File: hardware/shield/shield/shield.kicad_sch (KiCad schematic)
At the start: 4 parts, among them J3 Analog, J4 Digital/PWM, P1 Digital/PWM

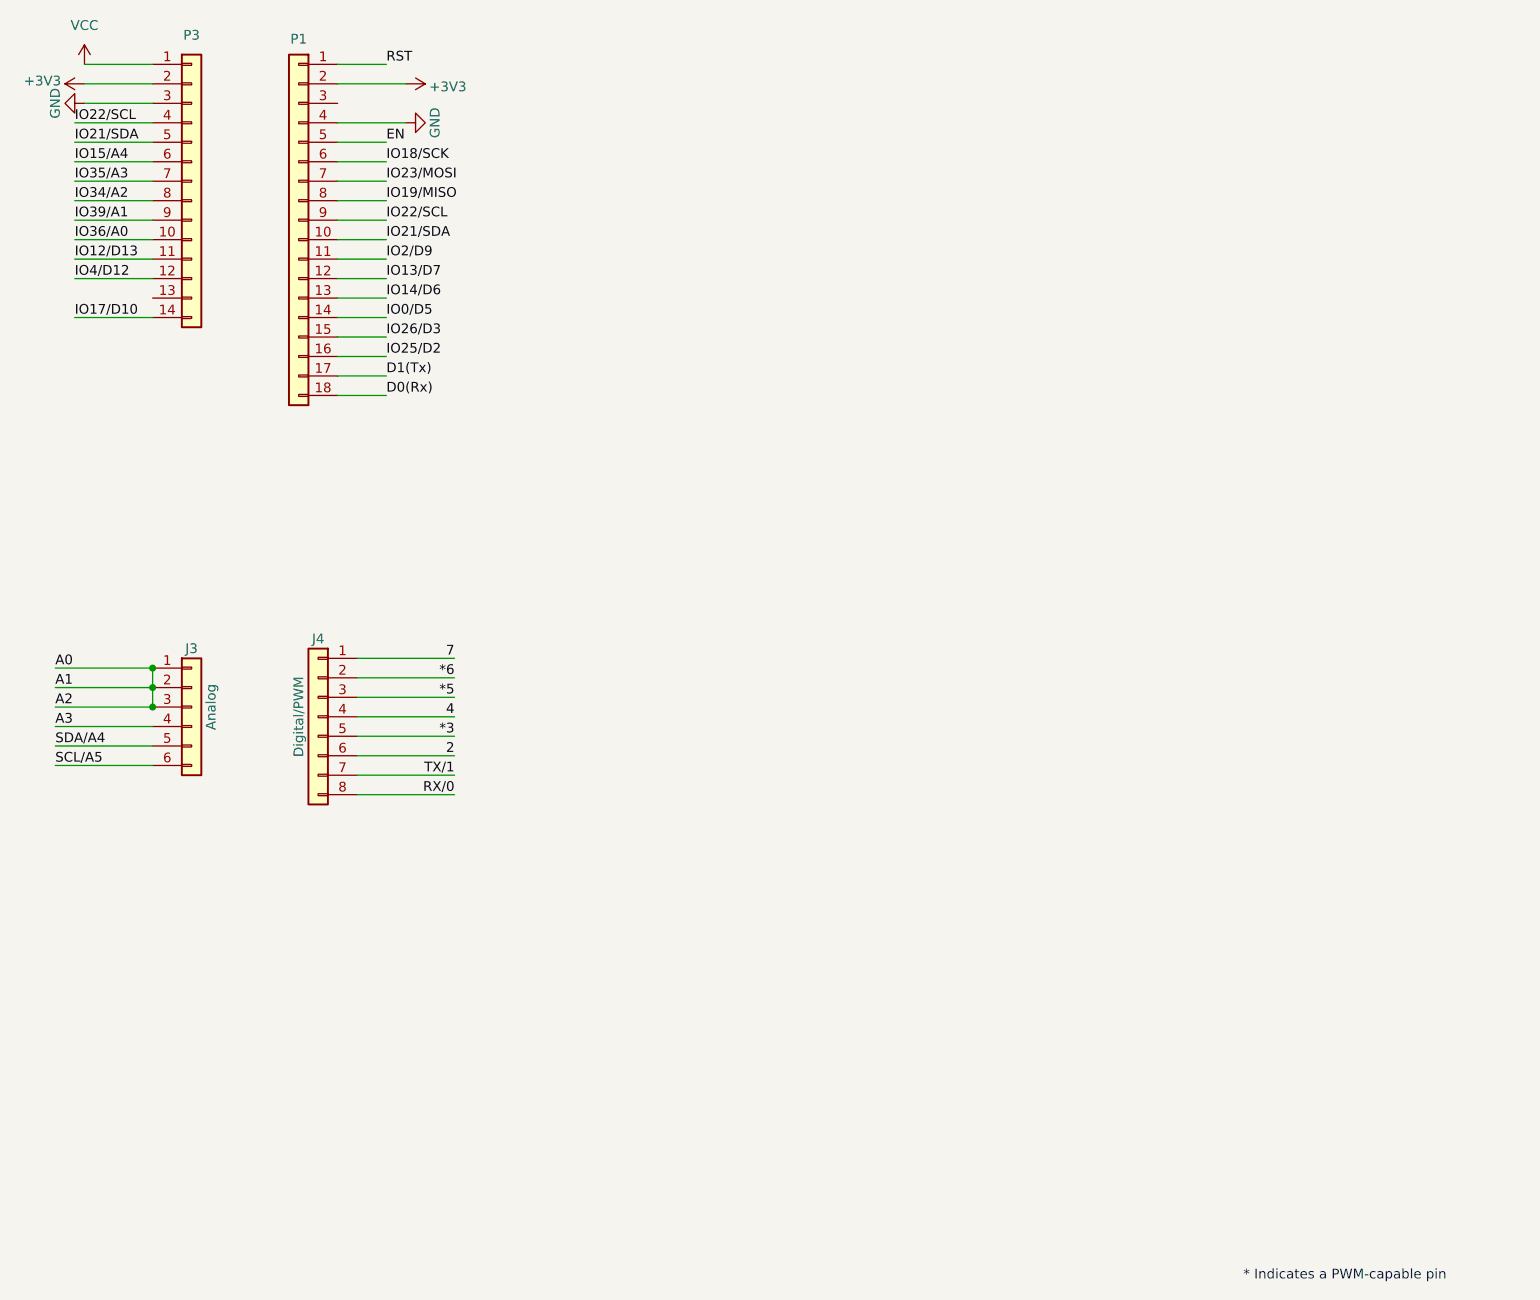
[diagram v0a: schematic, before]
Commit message: add pins for in/out
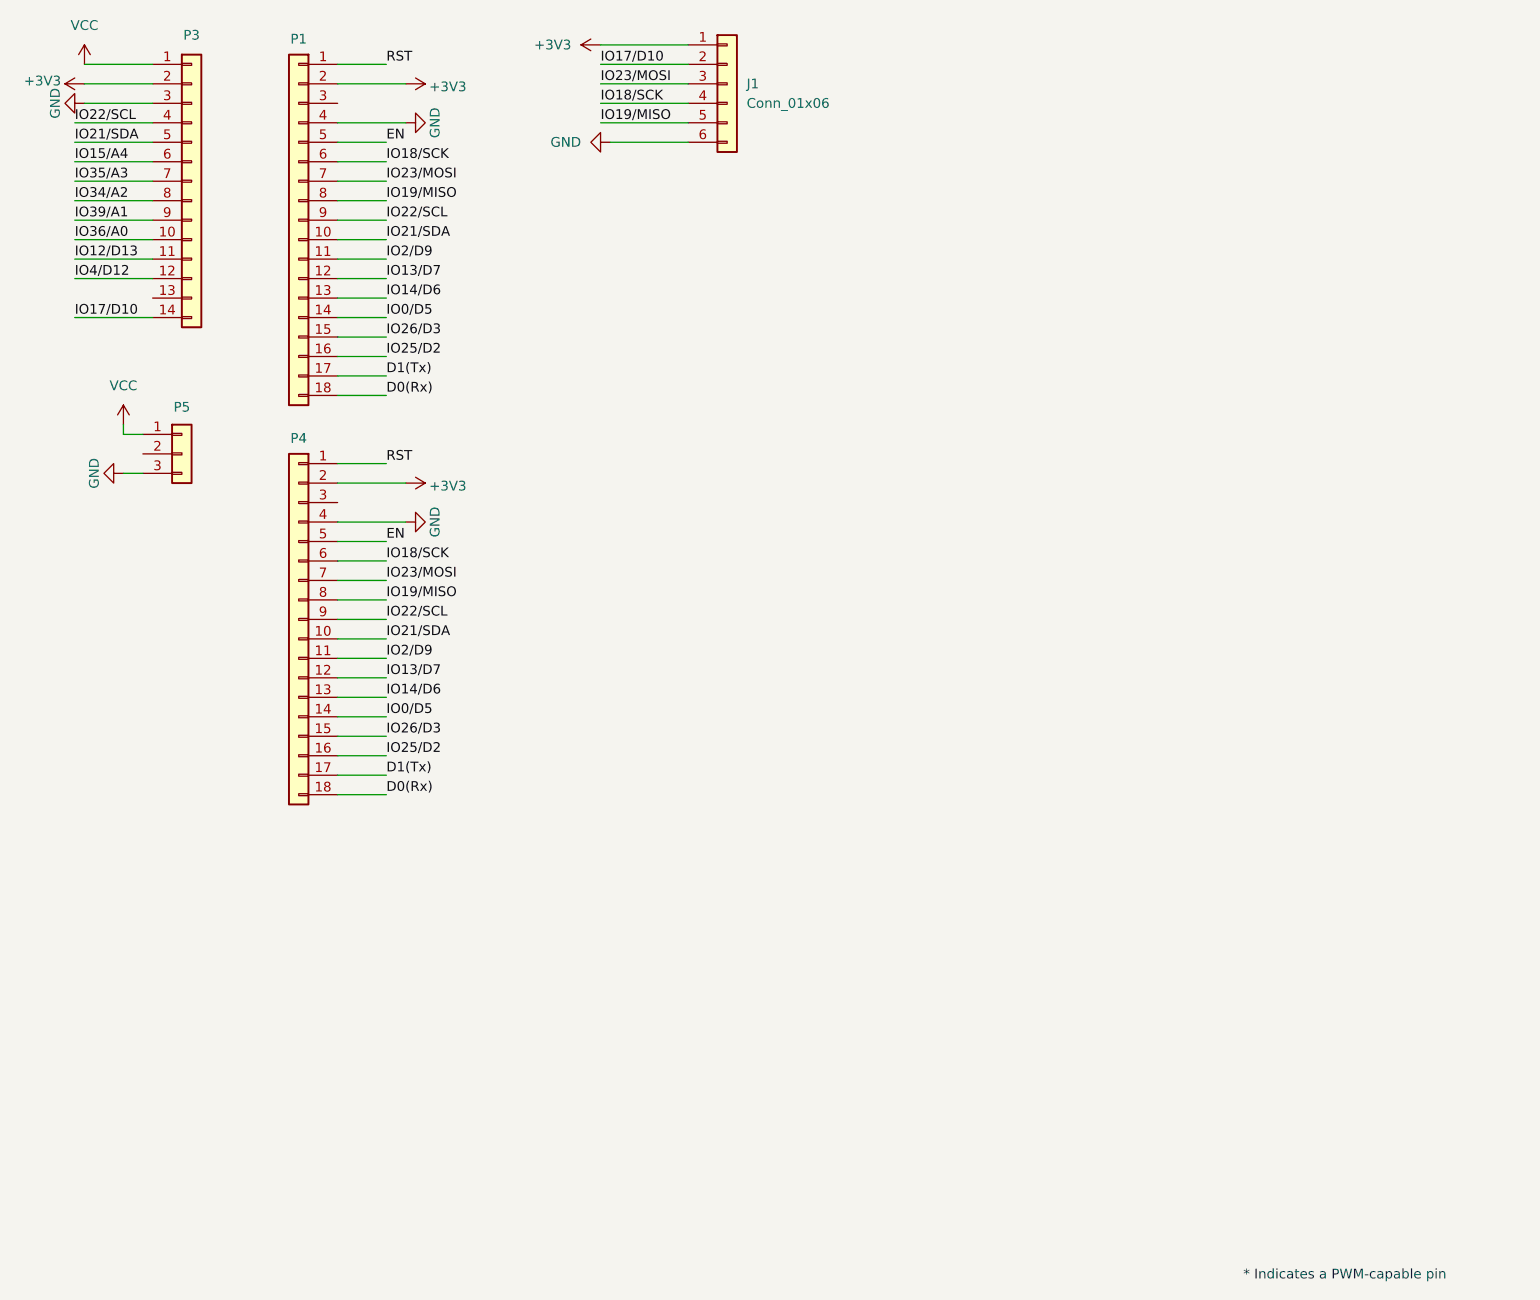
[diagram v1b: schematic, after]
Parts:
- removed J3: Analog, Connector_PinSocket_2.54mm:PinSocket_1x06_P2.54mm_Vertical, symbol Connector_Generic:Conn_01x06
- removed J4: Digital/PWM, Connector_PinSocket_2.54mm:PinSocket_1x08_P2.54mm_Vertical, symbol Connector_Generic:Conn_01x08
- added J1: Conn_01x06, Connector_PinHeader_2.54mm:PinHeader_1x06_P2.54mm_Horizontal, symbol Connector_Generic:Conn_01x06
- added P4: Digital/PWM, Connector_PinHeader_2.54mm:PinHeader_1x18_P2.54mm_Horizontal, symbol Connector_Generic:Conn_01x18
- added P5: ~, Connector_PinHeader_2.54mm:PinHeader_1x03_P2.54mm_Horizontal, symbol Connector_Generic:Conn_01x03
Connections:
- net +3V3: now also J1.1 (Pin_1), P4.2 (Pin_2)
- net D0(Rx): now also P4.18 (Pin_18)
- net D1(Tx): now also P4.17 (Pin_17)
- net EN: now also P4.5 (Pin_5)
- net GND: now also J1.6 (Pin_6), P4.4 (Pin_4), P5.3 (Pin_3)
- net IO0/D5: now also P4.14 (Pin_14)
- net IO13/D7: now also P4.12 (Pin_12)
- net IO14/D6: now also P4.13 (Pin_13)
- net IO17/D10: now also J1.2 (Pin_2)
- net IO18/SCK: now also J1.4 (Pin_4), P4.6 (Pin_6)
- net IO19/MISO: now also J1.5 (Pin_5), P4.8 (Pin_8)
- net IO21/SDA: now also P4.10 (Pin_10)
- net IO22/SCL: now also P4.9 (Pin_9)
- net IO23/MOSI: now also J1.3 (Pin_3), P4.7 (Pin_7)
- net IO25/D2: now also P4.16 (Pin_16)
- net IO26/D3: now also P4.15 (Pin_15)
- net IO2/D9: now also P4.11 (Pin_11)
- net RST: now also P4.1 (Pin_1)
- net VCC: now also P5.1 (Pin_1)

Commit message: add shield 0.3.1 version
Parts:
- added P6: ~, Connector_PinHeader_2.54mm:PinHeader_1x03_P2.54mm_Horizontal, symbol Connector_Generic:Conn_01x03
- added P7: ~, Connector_PinHeader_2.54mm:PinHeader_1x05_P2.54mm_Horizontal, symbol Connector_Generic:Conn_01x05
- added U1: LF33_TO252, Package_TO_SOT_SMD:TO-252-2, symbol Regulator_Linear:LF33_TO252
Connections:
- net GND: now also P6.3 (Pin_3), P7.1 (Pin_1), U1.2 (GND)
- net IO12/D13: now also P7.4 (Pin_4)
- net IO36/A0: now also P7.3 (Pin_3)
- net IO39/A1: now also P7.2 (Pin_2)
- net IO4/D12: now also P7.5 (Pin_5)
- net VCC: now also U1.1 (VI)
- new net +3.3V: P6.1 (Pin_1), U1.3 (VO)
